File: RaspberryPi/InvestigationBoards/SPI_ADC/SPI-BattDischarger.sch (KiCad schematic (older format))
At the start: 36 parts, among them J1 DB9, P1 CONN_20, P2 TST, P3 CONN_13X2, P4 CONN_2, Q1 NPN, Q2 NPN, Q3 NPN, Q4 NPN, U1 MAX146, U2 LM7805, U3 DS18B20

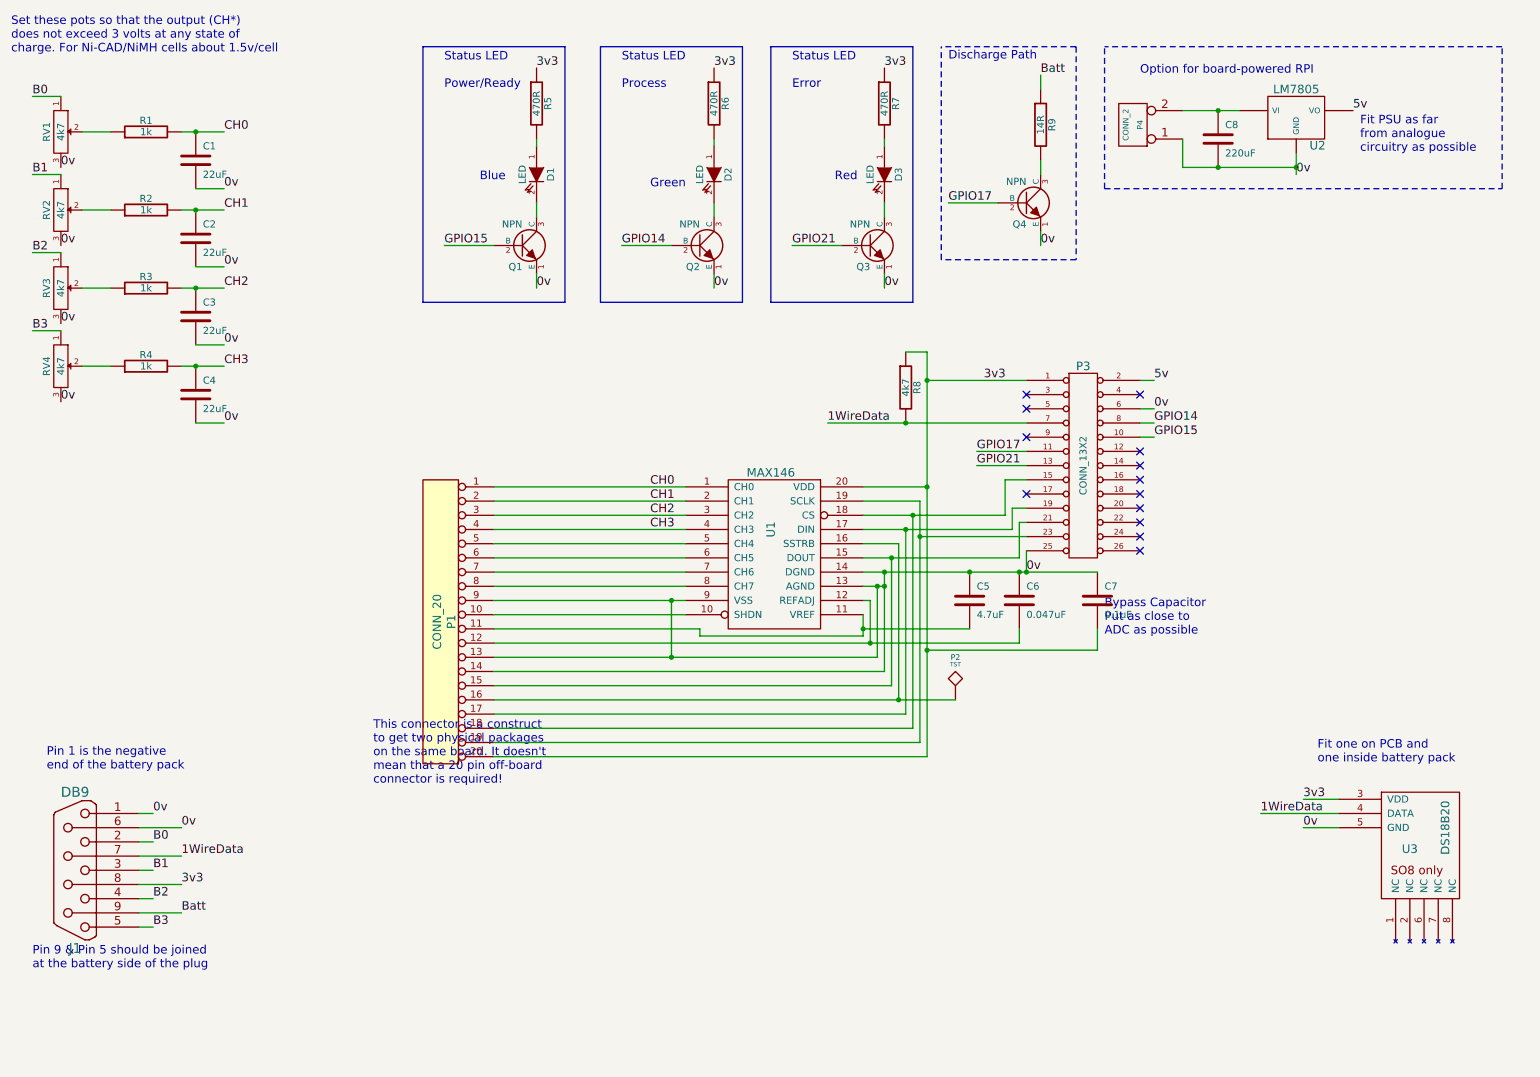
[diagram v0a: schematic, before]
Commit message: Updates to SPI ADC driver and hardware
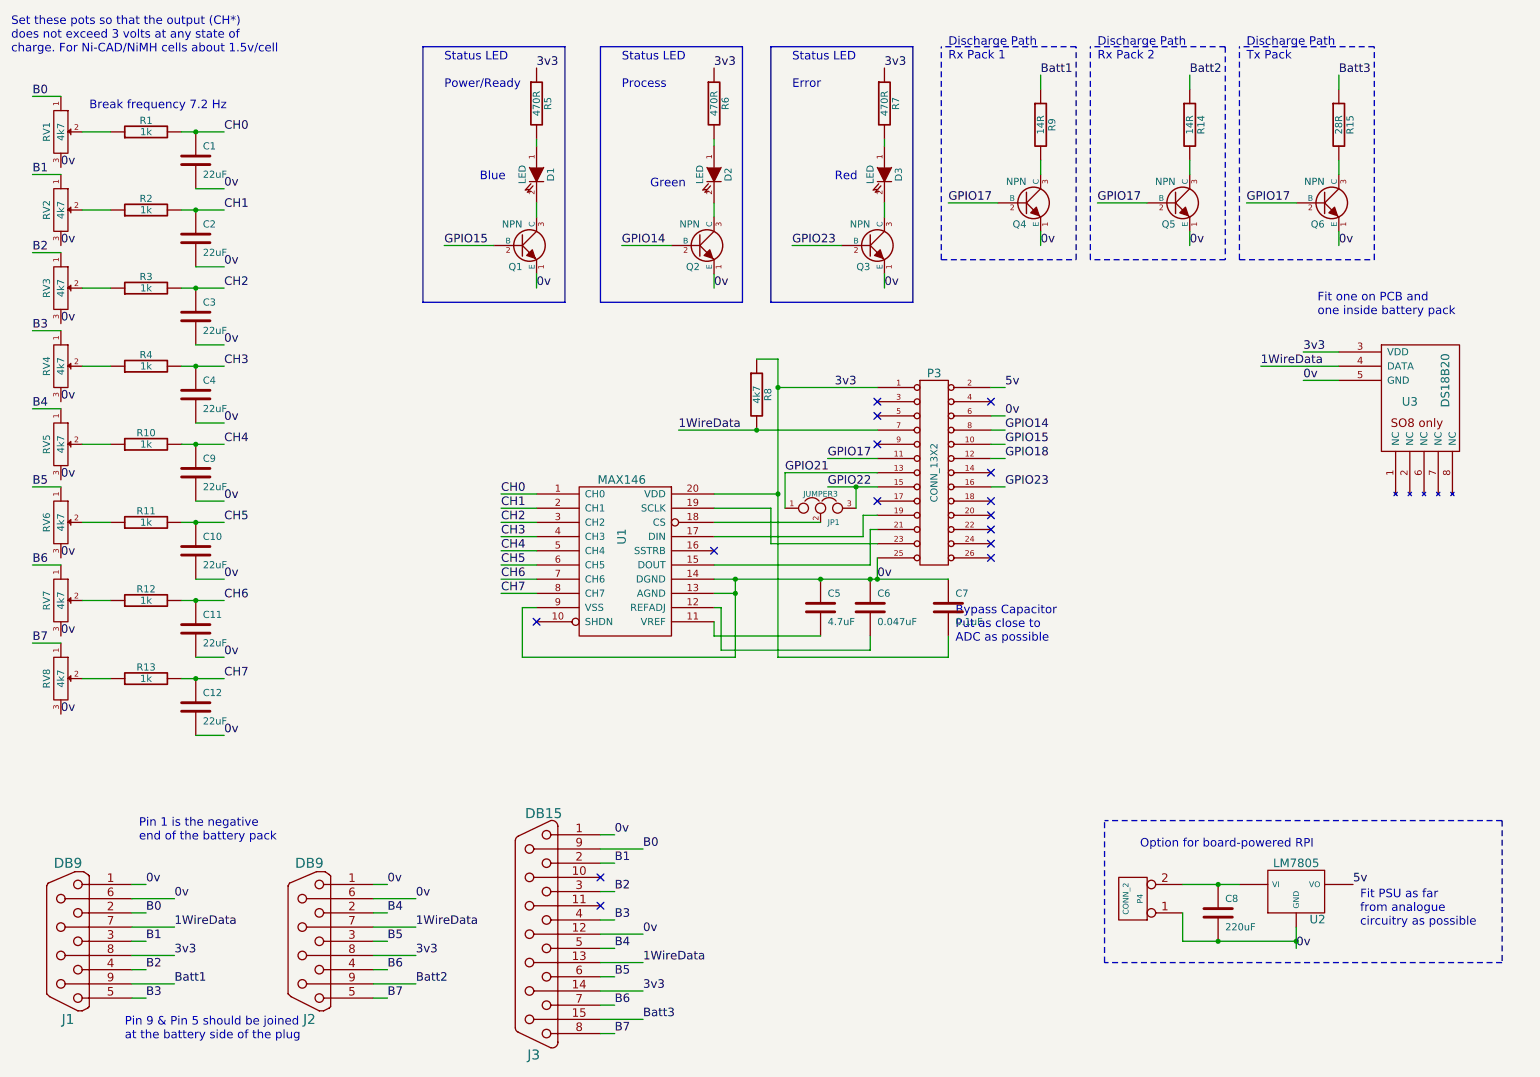
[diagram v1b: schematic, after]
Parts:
- removed P1: CONN_20, symbol CONN_20
- removed P2: TST, symbol TST
- added C10, C11, C12, C9: 22uF, symbol C
- added J2: DB9, symbol DB9
- added J3: DB15, symbol DB15
- added JP1: JUMPER3, symbol JUMPER3
- added Q5, Q6: NPN, symbol NPN
- added R10, R11, R12, R13: 1k, symbol R
- added R14: 14R, symbol R
- added R15: 28R, symbol R
- added RV5, RV6, RV7, RV8: 4k7, symbol POT
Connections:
- net 0v: now also C10.2, C11.2, C12.2, C9.2, J2.1, J2.6 (P6), J3.1, J3.12 (P12), Q5.1 (E), Q6.1 (E), RV5.3, RV6.3, RV7.3, RV8.3
- net 1WireData: now also J2.7 (P7), J3.13 (P13)
- net 3v3: now also J2.8 (P8), J3.14 (P14)
- net B0: now also J3.9 (P9)
- net B1: now also J3.2
- net B2: now also J3.3
- net B3: now also J3.4
- net GPIO17: now also Q5.2 (B), Q6.2 (B)
- net GPIO21: now also JP1.1; no longer Q3.2 (B)
- net at U1.18 (CS): now also JP1.2; no longer P3.15 (P15)
- net CH4: now reaches U1.5 (CH4)
- net CH4: now also C9.1, R10.2
- net CH5: now reaches U1.6 (CH5)
- net CH5: now also C10.1, R11.2
- net CH6: now reaches U1.7 (CH6)
- net CH6: now also C11.1, R12.2
- net CH7: now reaches U1.8 (CH7)
- net CH7: now also C12.1, R13.2
- net GPIO18: now reaches P3.12 (P12)
- net GPIO23: now reaches P3.16 (P16)
- net GPIO23: now also Q3.2 (B)
- net Batt renamed Batt1
- new net: R12.1, RV7.2
- new net: R13.1, RV8.2
- new net: R11.1, RV6.2
- new net: R10.1, RV5.2
- new net: Q5.3 (C), R14.2
- new net: Q6.3 (C), R15.2
- new net B4: J2.2, J3.5, RV5.1
- new net B5: J2.3, J3.6, RV6.1
- new net B6: J2.4, J3.7, RV7.1
- new net B7: J2.5, J3.8, RV8.1
- new net Batt2: J2.9 (P9), R14.1
- new net Batt3: J3.15 (P15), R15.1
- new net GPIO22: JP1.3, P3.15 (P15)
- no-connect marks 13 -> 15
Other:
- note added: "Break frequency 7.2 Hz"
- note added: "Discharge Path\nRx Pack 1"
- note added: "Discharge Path\nRx Pack 2"
- note added: "Discharge Path\nTx Pack"
- note removed: "Discharge Path"
- note removed: "This connector is a construct\nto get two physical packages\non the same board. It doesn't\nmean that a 20 pin off-board\nconnector is required!"
- moved on the sheet: C5, C6, C7, C8, J1, P3, P4, R8, U1, U2, U3
